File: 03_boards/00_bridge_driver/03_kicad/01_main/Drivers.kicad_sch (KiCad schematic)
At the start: 46 parts, among them Q1 SUD90330E, Q2 SUD90330E, Q3 SUD90330E, Q4 SUD90330E, Q5 SUD90330E, Q6 SUD90330E, U1 IRS2104, U2 IRS2104, U3 IRS2104, U4 ISO7740DWR

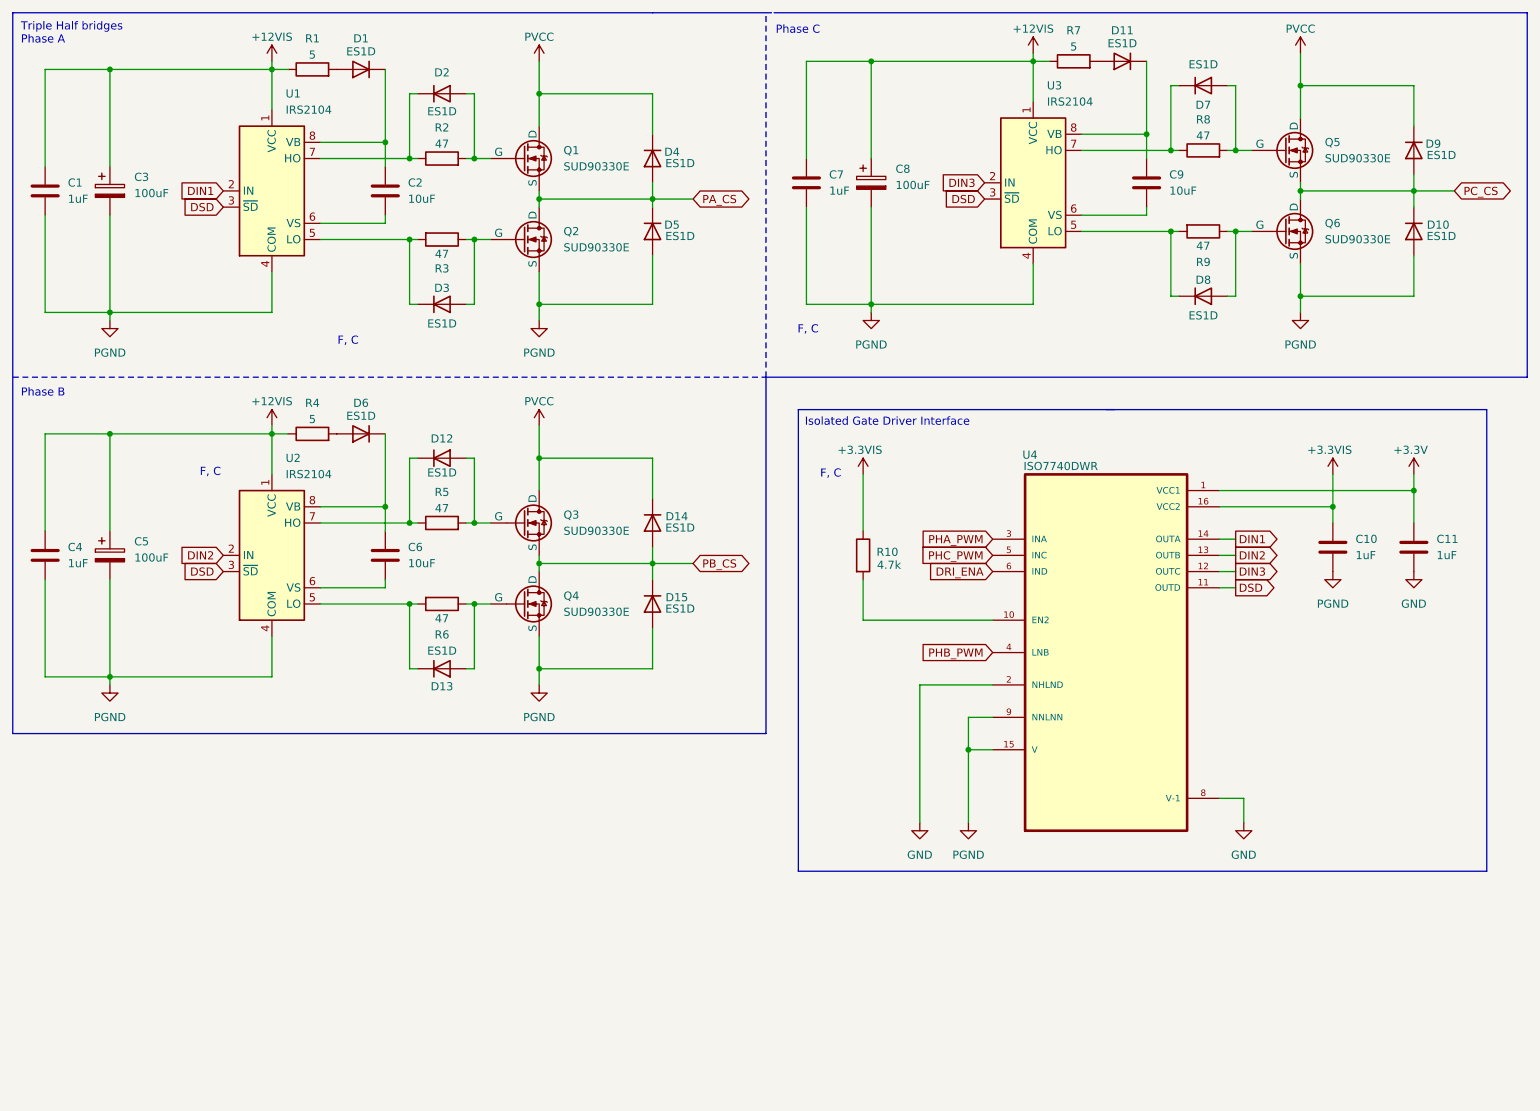
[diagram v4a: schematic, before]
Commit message: Week 0x9 | Nearly there! (#38)
* Updated readmes formatting & other files

* Removed no commercial aspiration notes and added a simple status section for the readme

* Made the status section inline

* Forgot a full stop.

* Added application notes to docs/readme.md

* Added current state and terminal state on the application notes series

* Added .md instead of .csv for BOM

* Added BOM for bridge driver and updated the - to em

* Added 04_procurement folders and made 04_media into 05_media

* Added fixture folder and moved docs to 00

* Technically I have done that just by the bridge driver design.

* Added checking system for BOM and added 05_media section for bridge driver

* Added the order for magnetic encoder

* Added the the link to the digikey file.

* Updated media & readmes to reflect that

* Got the digikey BOM and also checked the list off for armature board

* Nearly finished the schematic for driver board

* Added a some code and fixed the derived.ut vs metric.ut referencing mistake

* Finished Driver Board Schematic.

* More footprint selection. YAY

* More footprints.

* Footprints finished and hence initial BOM based on footprints is also

* Updated schematic.

* Improving the unit boundary and notes for 00_analytical

* Updated main readme to reflect work done this week.

* Removed the line about the integrated sensor board. it's literally below it.

* Rewrote fabrication note.

* Update README.md

* Updated readmes and added the bowley system logo

* Made it clear the values and updated the schematics.

* Updated comment to design not development. they mean different things.

* deleted .csv -> Who uses it anyways!?

* Initial PCB modelling work

* Added work so far on bridge driver. Took some pics and updates readmes.

* Updated to doubles images (back and front)
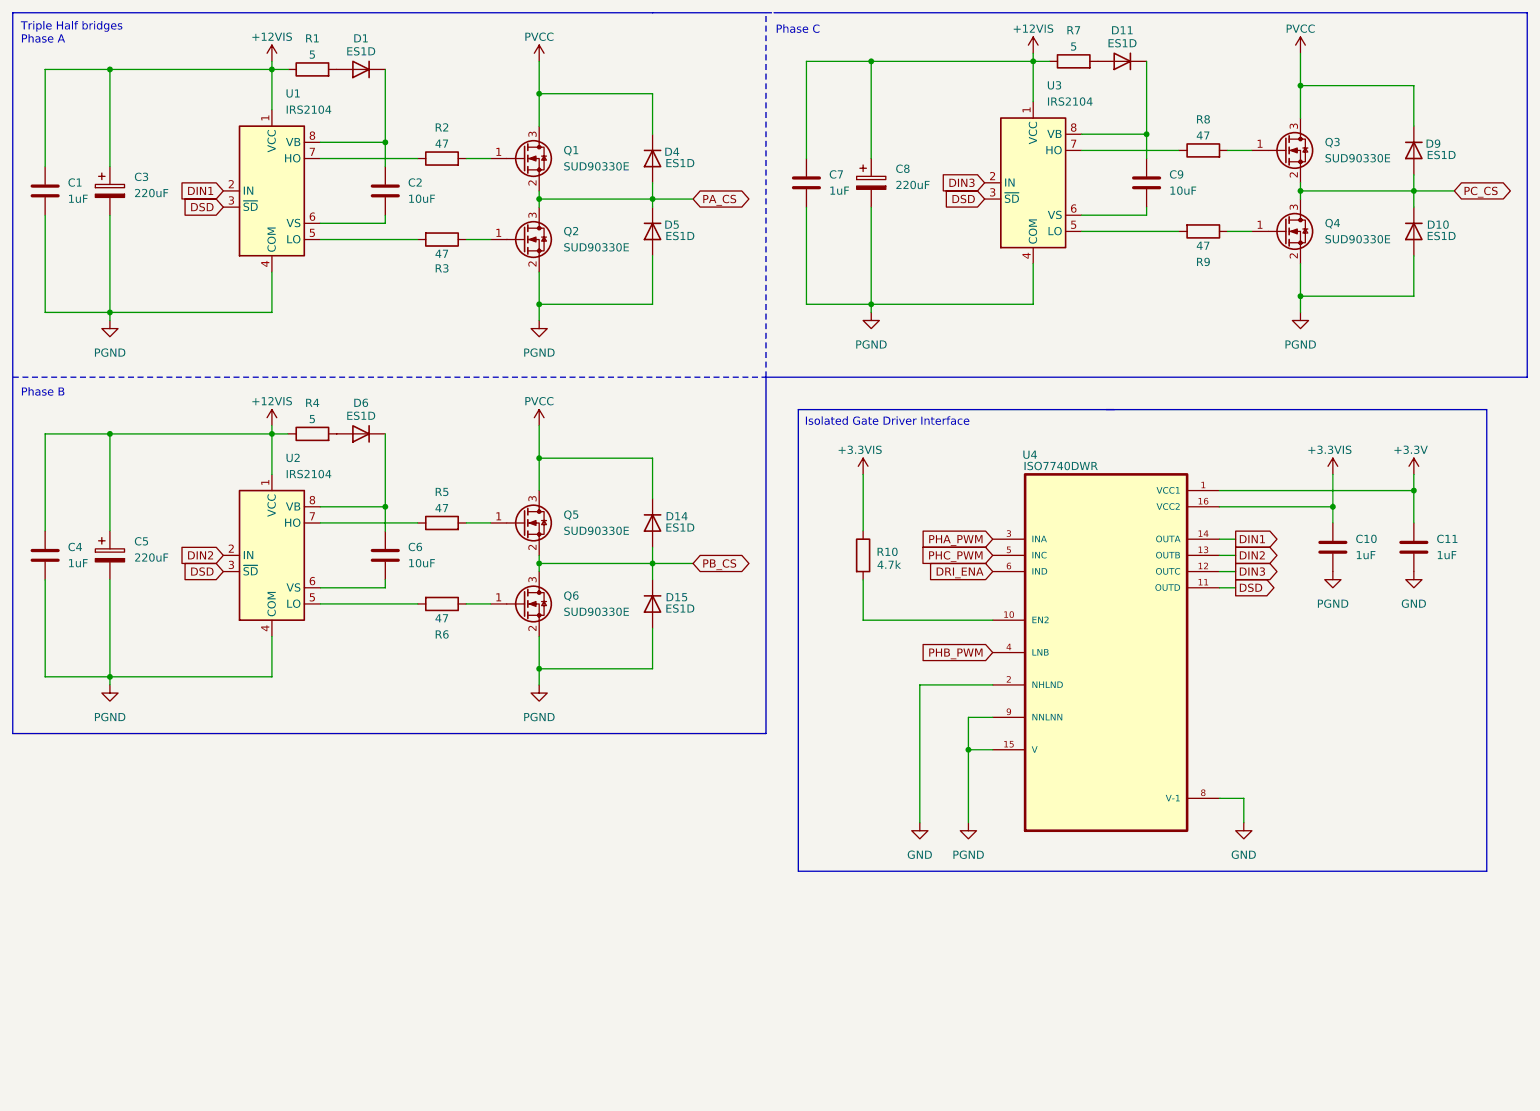
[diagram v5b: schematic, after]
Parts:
- removed D12, D13, D2, D3, D7, D8: ES1D, symbol Device:D
- removed Q1, Q2, Q3, Q4, Q5, Q6: SUD90330E, symbol Simulation_SPICE:NMOS
- added Q1, Q2, Q3, Q4, Q5, Q6: SUD90330E, sud90330e:TO-252-2, symbol Transistor_FET:Q_NMOS_GSD
- C1, C10, C11, C4, C7: footprint (none) -> Capacitor_SMD:C_0603_1608Metric
- C2, C6, C9: footprint (none) -> Capacitor_SMD:C_1206_3216Metric
- C3, C5, C8: value 100uF -> 220uF; footprint (none) -> Capacitor_THT:CP_Radial_D8.0mm_P3.50mm
- D1, D10, D11, D14, D15, D4, D5, D6, D9: footprint (none) -> ES1D:DIOM4325X250N
- R1, R10, R4, R7: footprint (none) -> Resistor_SMD:R_0603_1608Metric
- R2, R3, R5, R6, R8, R9: footprint (none) -> Resistor_SMD:R_1206_3216Metric
- U1, U2, U3: footprint (none) -> Package_SO:SOIC-8_3.9x4.9mm_P1.27mm
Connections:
- net PA_CS: now also Q1.2 (S), Q2.3 (D)
- net PB_CS: now also Q5.2 (S), Q6.3 (D)
- net PC_CS: now also Q3.2 (S), Q4.3 (D)
- net PGND: now also Q2.2 (S), Q4.2 (S), Q6.2 (S)
- net PVCC: now also Q1.3 (D), Q3.3 (D), Q5.3 (D)
- net at R8.2: now also Q3.1 (G)
- net at R2.2: now also Q1.1 (G)
- net at R5.2: now also Q5.1 (G)
- net at R9.1: now also Q4.1 (G)
- net at R3.1: now also Q2.1 (G)
- net at R6.1: now also Q6.1 (G)
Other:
- note removed: "F, C"
